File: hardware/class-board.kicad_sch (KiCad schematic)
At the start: 0 parts

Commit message: hardware: panel stacked on the back (180 x 100, three 2x20 headers, 17 SMA, TTL strip, TX terminal, Qwiic); TTL/fast/TX-coil/Qwiic connectors leave the main board; mains-safe relay channels (JQC-3FF 10 A, MAINS net class + DRC rules); library, sheets, gapped copies, docs regenerated; ERC 0 errors
Decisions #45-#50 in the course repo. The main-board PCB is unchanged: Update PCB from Schematic, header placement, relay re-spacing and connector rotation are the instructor's GUI steps on the master.

Co-Authored-By: Claude Fable 5.1 <noreply@anthropic.com>
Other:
- note added: "400 kHz: OLED 0x3C, TCA9535 0x20, Si5351A 0x60, Qwiic J4 + panel Qwiic"
- note added: "74AHCT541 -> 1 k -> panel link -> panel TTL strip"
- note added: "74HCT125 -> 49.9 R -> panel link -> 2 fast SMAs on the panel"
- note added: "74LVC1T45; DIR 1 = output to the panel SMA"
- note added: "<= 1.5 A (est. 1.15-1.35 A)"
- note added: "L1/L4 analog copper, panel copper (through J6)"
- note added: "LINK: 3 x 2x20 to the front panel (bottom side)"
- note added: "Stack-up: L1 signal/power, L2 GND, L3 GND, L4 signal/power. Board 180 x 100 mm, 4 x M3. Bottom side: three 2x20 straight male headers (J6 at x 12, J7 at x 90, J8 at x 168 mm) carry the front panel (180 x 100, 17 SMA) flat on the back of the board. Rear edge: USB-C, 5 V jack, relay contacts, isolated inputs, external power, H-bridge and polarizer coil terminals. Sections: A = B1 + NMR RX, B = B3 +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"
- note added: "dev board, relays (4 x 71 mA), 5 V logic, LDO, DC-DC"
- note removed: "400 kHz: OLED 0x3C, TCA9535 0x20, Si5351A 0x60, 2 Qwiic"
- note removed: "74AHCT541 -> 1 k -> terminals (I2C expander)"
- note removed: "74HCT125 -> 49.9 R -> terminals"
- note removed: "74LVC1T45; DIR 1 = output to the SMA"
- note removed: "<= 1.5 A (est. 1.0-1.2 A)"
- note removed: "L1/L4 analog copper, panel copper"
- note removed: "LINK: 2x20 to the front panel"
- note removed: "Stack-up: L1 signal/power, L2 GND, L3 GND, L4 signal/power. Board 160 x 100 mm, 4 x M3. Front edge: 2x20 link to the SMA/OLED/LED panel (160 x 65, 3 x 5 SMA). Rear edge: USB-C, 5 V jack, terminals, external power. Sections: A = B1 + NMR RX, B = B3 + B5 + NMR TX, C = B2 + B4 + coil switches."
- note removed: "dev board, relays, 5 V logic, LDO, DC-DC"
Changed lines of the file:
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@@
   (text "TIGP CLASS BOARD 2026 — laboratory instrument carrier (ESP32-S3 dev board) with NMR console, rev B (v0.7, 2026-09-13)" (exclude_from_sim no) (at 12.7 16 0) (effects (font (size 3.5 3.5) (bold yes)) (justify left bottom)))
   (text "Design brief v0.6 + notes/2026-09-13-nmr-respec-proposal.md (v0.7) + hardware/docs/design-decisions.md. Interface nets between sheets are global labels; rails are power symbols; AGND meets GND only at NT1." (exclude_from_sim no) (at 12.7 21 0) (effects (font (size 1.5 1.5)) (justify left bottom)))
-  (text "Stack-up: L1 signal/power, L2 GND, L3 GND, L4 signal/power. Board 160 x 100 mm, 4 x M3. Front edge: 2x20 link to the SMA/OLED/LED panel (160 x 65, 3 x 5 SMA). Rear edge: USB-C, 5 V jack, terminals, external power. Sections: A = B1 + NMR RX, B = B3 + B5 + NMR TX, C = B2 + B4 + coil switches." (exclude_from_sim no) (at 12.7 25 0) (effects (font (size 1.5 1.5)) (justify left bottom)))
+  (text "Stack-up: L1 signal/power, L2 GND, L3 GND, L4 signal/power. Board 180 x 100 mm, 4 x M3. Bottom side: three 2x20 straight male headers (J6 at x 12, J7 at x 90, J8 at x 168 mm) carry the front panel (180 x 100, 17 SMA) flat on the back of the board. Rear edge: USB-C, 5 V jack, relay contacts, isolated inputs, external power, H-bridge and polarizer coil terminals. Sections: A = B1 + NMR RX, B = B3 + B5 + NMR TX, C = B2 + B4 + coil switches." (exclude_from_sim no) (at 12.7 25 0) (effects (font (size 1.5 1.5)) (justify left bottom)))
   (text "BASE: dev-board socket, buses, expansion, star point" (exclude_from_sim no) (at 14.2 62 0) (effects (font (size 1.3 1.3)) (justify left bottom)))
   (text "B2 (C): power entry, +-12 V, LDOs" (exclude_from_sim no) (at 114.2 62 0) (effects (font (size 1.3 1.3)) (justify left bottom)))
@@
   (text "B4 (C): 4 relays, 2 isolated inputs" (exclude_from_sim no) (at 14.2 107 0) (effects (font (size 1.3 1.3)) (justify left bottom)))
   (text "B5 (B): TCA9535 -> 8 TTL DIO + relays, 2 fast outs, TRIG" (exclude_from_sim no) (at 114.2 107 0) (effects (font (size 1.3 1.3)) (justify left bottom)))
-  (text "LINK: 2x20 to the front panel" (exclude_from_sim no) (at 214.2 107 0) (effects (font (size 1.3 1.3)) (justify left bottom)))
+  (text "LINK: 3 x 2x20 to the front panel (bottom side)" (exclude_from_sim no) (at 214.2 107 0) (effects (font (size 1.3 1.3)) (justify left bottom)))
   (text "C: external power input, DRV8871 field-cycling H-bridge, polarizer MOSFET switch" (exclude_from_sim no) (at 314.2 107 0) (effects (font (size 1.3 1.3)) (justify left bottom)))
   (text "NMR RX (A): tank, LNA, blanking, I/Q mixer, IF -> ADC ch 7/8" (exclude_from_sim no) (at 14.2 152 0) (effects (font (size 1.3 1.3)) (justify left bottom)))
@@
   (text "1/2" (exclude_from_sim no) (at 13.5 193.4992 0) (effects (font (size 1.3 1.3)) (justify left bottom)))
   (text "I2C_SDA/SCL" (exclude_from_sim no) (at 47.5 193.4992 0) (effects (font (size 1.3 1.3)) (justify left bottom)))
-  (text "400 kHz: OLED 0x3C, TCA9535 0x20, Si5351A 0x60, 2 Qwiic" (exclude_from_sim no) (at 87.5 193.4992 0) (effects (font (size 1.3 1.3)) (justify left bottom)))
+  (text "400 kHz: OLED 0x3C, TCA9535 0x20, Si5351A 0x60, Qwiic J4 + panel Qwiic" (exclude_from_sim no) (at 87.5 193.4992 0) (effects (font (size 1.3 1.3)) (justify left bottom)))
   (text "base" (exclude_from_sim no) (at 179.5 193.4992 0) (effects (font (size 1.3 1.3)) (justify left bottom)))
   (text "16/17" (exclude_from_sim no) (at 13.5 196.3592 0) (effects (font (size 1.3 1.3)) (justify left bottom)))
@@
   (text "18/21" (exclude_from_sim no) (at 13.5 199.2192 0) (effects (font (size 1.3 1.3)) (justify left bottom)))
   (text "FAST_OUT1/2" (exclude_from_sim no) (at 47.5 199.2192 0) (effects (font (size 1.3 1.3)) (justify left bottom)))
-  (text "74HCT125 -> 49.9 R -> terminals" (exclude_from_sim no) (at 87.5 199.2192 0) (effects (font (size 1.3 1.3)) (justify left bottom)))
+  (text "74HCT125 -> 49.9 R -> panel link -> 2 fast SMAs on the panel" (exclude_from_sim no) (at 87.5 199.2192 0) (effects (font (size 1.3 1.3)) (justify left bottom)))
   (text "B" (exclude_from_sim no) (at 179.5 199.2192 0) (effects (font (size 1.3 1.3)) (justify left bottom)))
   (text "38/39" (exclude_from_sim no) (at 13.5 202.0792 0) (effects (font (size 1.3 1.3)) (justify left bottom)))
   (text "TRIG_IO / TRIG_DIR" (exclude_from_sim no) (at 47.5 202.0792 0) (effects (font (size 1.3 1.3)) (justify left bottom)))
-  (text "74LVC1T45; DIR 1 = output to the SMA" (exclude_from_sim no) (at 87.5 202.0792 0) (effects (font (size 1.3 1.3)) (justify left bottom)))
+  (text "74LVC1T45; DIR 1 = output to the panel SMA" (exclude_from_sim no) (at 87.5 202.0792 0) (effects (font (size 1.3 1.3)) (justify left bottom)))
   (text "B" (exclude_from_sim no) (at 179.5 202.0792 0) (effects (font (size 1.3 1.3)) (justify left bottom)))
   (text "41/42" (exclude_from_sim no) (at 13.5 204.9392 0) (effects (font (size 1.3 1.3)) (justify left bottom)))
@@
   (text "TCA9535 P00-P07" (exclude_from_sim no) (at 13.5 219.2392 0) (effects (font (size 1.3 1.3)) (justify left bottom)))
   (text "DIO1..8" (exclude_from_sim no) (at 47.5 219.2392 0) (effects (font (size 1.3 1.3)) (justify left bottom)))
-  (text "74AHCT541 -> 1 k -> terminals (I2C expander)" (exclude_from_sim no) (at 87.5 219.2392 0) (effects (font (size 1.3 1.3)) (justify left bottom)))
+  (text "74AHCT541 -> 1 k -> panel link -> panel TTL strip" (exclude_from_sim no) (at 87.5 219.2392 0) (effects (font (size 1.3 1.3)) (justify left bottom)))
   (text "B" (exclude_from_sim no) (at 179.5 219.2392 0) (effects (font (size 1.3 1.3)) (justify left bottom)))
   (text "TCA9535 P10-P13" (exclude_from_sim no) (at 13.5 222.0992 0) (effects (font (size 1.3 1.3)) (justify left bottom)))
@@
   (text "+5V_RAW" (exclude_from_sim no) (at 200.8 184.9192 0) (effects (font (size 1.3 1.3)) (justify left bottom)))
   (text "USB-C or jack via polyfuse + TVS + LM66100" (exclude_from_sim no) (at 226.8 184.9192 0) (effects (font (size 1.3 1.3)) (justify left bottom)))
-  (text "<= 1.5 A (est. 1.0-1.2 A)" (exclude_from_sim no) (at 288.8 184.9192 0) (effects (font (size 1.3 1.3)) (justify left bottom)))
-  (text "dev board, relays, 5 V logic, LDO, DC-DC" (exclude_from_sim no) (at 340.8 184.9192 0) (effects (font (size 1.3 1.3)) (justify left bottom)))
+  (text "<= 1.5 A (est. 1.15-1.35 A)" (exclude_from_sim no) (at 288.8 184.9192 0) (effects (font (size 1.3 1.3)) (justify left bottom)))
+  (text "dev board, relays (4 x 71 mA), 5 V logic, LDO, DC-DC" (exclude_from_sim no) (at 340.8 184.9192 0) (effects (font (size 1.3 1.3)) (justify left bottom)))
   (text "+3V3" (exclude_from_sim no) (at 200.8 187.7792 0) (effects (font (size 1.3 1.3)) (justify left bottom)))
   (text "AMS1117-3.3" (exclude_from_sim no) (at 226.8 187.7792 0) (effects (font (size 1.3 1.3)) (justify left bottom)))
@@
   (text "star point NT1 (net tie) to GND" (exclude_from_sim no) (at 226.8 196.3592 0) (effects (font (size 1.3 1.3)) (justify left bottom)))
   (text "-" (exclude_from_sim no) (at 288.8 196.3592 0) (effects (font (size 1.3 1.3)) (justify left bottom)))
-  (text "L1/L4 analog copper, panel copper" (exclude_from_sim no) (at 340.8 196.3592 0) (effects (font (size 1.3 1.3)) (justify left bottom)))
+  (text "L1/L4 analog copper, panel copper (through J6)" (exclude_from_sim no) (at 340.8 196.3592 0) (effects (font (size 1.3 1.3)) (justify left bottom)))
   (sheet (at 12.7 35.56) (size 88.9 30.48) (fields_autoplaced yes) (stroke (width 0.1524) (type solid)) (fill (color 0 0 0 0.0000))
     (property "Sheetname" "base_mcu" (at 12.7 34.86 0) (effects (font (size 1.5 1.5) (bold yes)) (justify left bottom)))

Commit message: v0.7d: relays and mains removed, MODULE OUT 1-7 (5 V TTL) on a shrouded 2x6 header on the front panel, isolated inputs moved to the panel, section C = the front-panel board (4-layer, 18 mm SMA grid, OLED clear of headers, unrouted student copy), main board re-placed; workbook, tutor guide, firmware docs, hardware docs updated (Decision #58)
Co-Authored-By: Claude Fable 5.1 <noreply@anthropic.com>
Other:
- removed sheet b4_switching
- note added: "/CLR of the 74HC74 Johnson counter (NMR RX); TP501"
- note added: "3.3 V -> panel link J8 -> 5 V TTL buffers on the panel (OUT 8 reserved, J8 pin 33 n/c)"
- note added: "<= 1.5 A (est. 0.87-1.07 A)"
- note added: "B5 (B): TCA9535 -> 8 TTL DIO + 8 module outputs, 2 fast outs, TRIG"
- note added: "EXP_P14"
- note added: "MODULE OUT 1..7"
- note added: "Reference ranges: base 1-99, B1 100-199, B2 200-299, B3 300-399, B5 500-599, NMR RX 700-799, NMR TX 800-899, coil switches / external power 900-999. B4 (400-499, relays and isolated inputs) was deleted in v0.7d; the owner-zone DRC uses the Block field."
- note added: "Stack-up: L1 signal/power, L2 GND, L3 GND, L4 signal/power. Board 180 x 100 mm, 4 x M3. Bottom side: three 2x20 straight male headers (J6 at x 12, J7 at x 90, J8 at x 168 mm) carry the front panel (180 x 100, 17 SMA) flat on the back of the board. Rear edge: USB-C, 5 V jack, external power, H-bridge and polarizer coil terminals. Sections: A = B1 + NMR RX, B = B3 + B5 + NMR TX, C = the front-panel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"
- note added: "TCA9535 P10-P13, P15-P17"
- note added: "TCA9535 P14"
- note added: "dev board, 5 V logic, LDO, DC-DC, the panel through J8"
- note added: "panel"
- note added: "the two isolated inputs, now on the front panel; active LOW"
- note removed: "6N137 outputs, 1 k pull-up, active LOW"
- note removed: "<= 1.5 A (est. 1.15-1.35 A)"
- note removed: "AO3400A relay gates (10 k pull-down)"
- note removed: "B4 (C): 4 relays, 2 isolated inputs"
- note removed: "B5 (B): TCA9535 -> 8 TTL DIO + relays, 2 fast outs, TRIG"
- note removed: "RLY_IN1..4"
- note removed: "Reference ranges: base 1-99, B1 100-199, B2 200-299, B3 300-399, B4 400-499, B5 500-599, NMR RX 700-799, NMR TX 800-899, coil switches / external power 900-999 (owner-zone DRC uses the Block field: A / B / C)."
- note removed: "Stack-up: L1 signal/power, L2 GND, L3 GND, L4 signal/power. Board 180 x 100 mm, 4 x M3. Bottom side: three 2x20 straight male headers (J6 at x 12, J7 at x 90, J8 at x 168 mm) carry the front panel (180 x 100, 17 SMA) flat on the back of the board. Rear edge: USB-C, 5 V jack, relay contacts, isolated inputs, external power, H-bridge and polarizer coil terminals. Sections: A = B1 + NMR RX, B = B3 +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"
- note removed: "TCA9535 P10-P13"
- note removed: "dev board, relays (4 x 71 mA), 5 V logic, LDO, DC-DC"

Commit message: Boards as hand-reworked by the instructor 2026-09-18 (Decision #66): three 2x20 links re-placed, jumpers -> headers, TCXO removed, 16 SMA; layout and routing in progress; review in the course repo notes
Co-Authored-By: Claude Fable 5.1 <noreply@anthropic.com>
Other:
- sheet b1_inputs ports: added AO1, AO2, AUX, COND_OUT1, COND_OUT2, CS_ADC, RX, TX; removed none
- sheet b2_power ports: added USB_D_N, USB_D_P; removed none
- sheet b3_outputs ports: added AO1, AO2, CS_DAC; removed none
- sheet b5_dio_trig ports: added EXP_P14, FAST_OUT1, FAST_OUT2, LED_ACT, LED_WIFI, OPTO_IN1, OPTO_IN2, TRIG_DIR, TRIG_IO; removed none
- sheet base_mcu ports: added CS_ADC, CS_DAC, DDS_FSYNC, DDS_PSEL, FAST_OUT1, FAST_OUT2, FET_GATE, HB_IN1, HB_IN2, LED_ACT, LED_WIFI, OPTO_IN1, OPTO_IN2, RX_BLANK, TRIG_DIR, TRIG_IO, TX_EN, USB_D_N, USB_D_P; removed none
- sheet c_switch ports: added FET_GATE, HB_IN1, HB_IN2; removed none
- sheet nmr_rx ports: added AUX, CLK0_MCLK, COND_OUT1, COND_OUT2, EXP_P14, RX, RX_BLANK; removed none
- sheet nmr_tx ports: added CLK0_MCLK, DDS_FSYNC, DDS_PSEL, TX, TX_EN; removed none

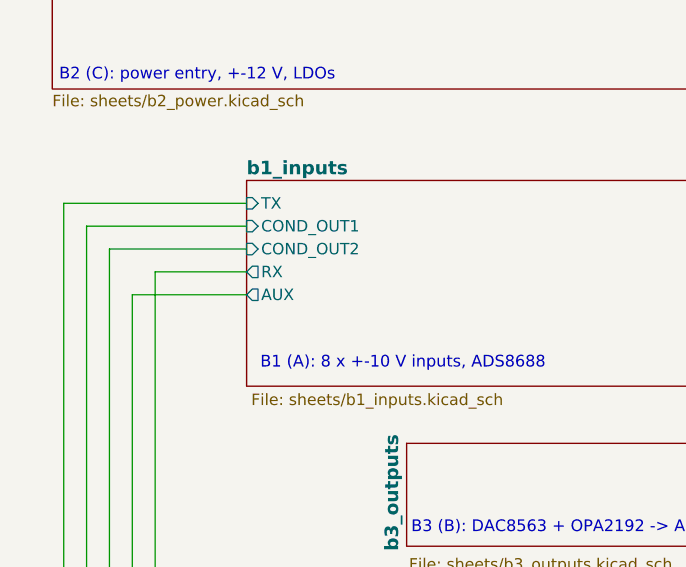
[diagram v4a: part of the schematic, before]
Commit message: Schematic review fixes, part 1 (branch, not merged): root sheet RX/AUX un-crossed + b1_inputs J6 pin 20/22 labels swapped (copper unchanged); firmware: ADC channel table kAinOfAi, FAST_OUT pins, module outputs 1-7 (relay -> module per PROTOCOL.md), AD9834 PIN/SW = 0, opto INPUT_PULLUP, stale comments; both PlatformIO envs build
Co-Authored-By: Claude Fable 5.1 <noreply@anthropic.com>
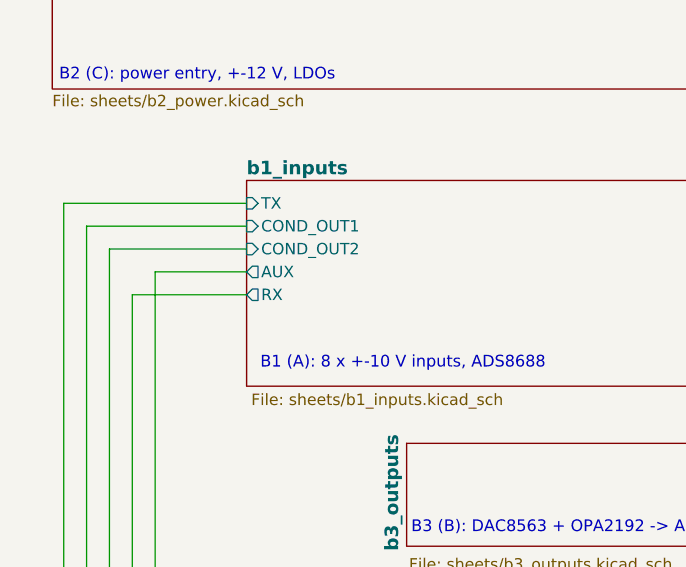
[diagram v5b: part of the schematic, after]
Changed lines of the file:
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@@
 			)
 		)
-		(pin "AUX" output
+		(pin "RX" output
 			(at 43.18 86.36 180)
 			(effects
@@
 			)
 		)
-		(pin "RX" output
+		(pin "AUX" output
 			(at 43.18 83.82 180)
 			(effects

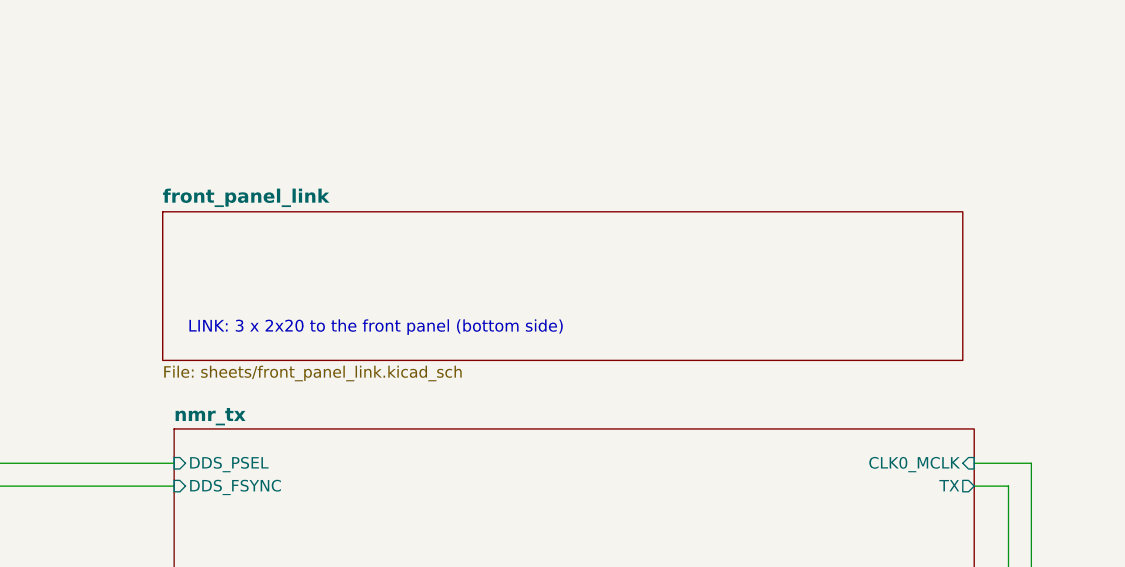
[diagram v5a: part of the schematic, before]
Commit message: Schematic review fixes, part 2 (Konnect): panel RX/AUX labels + SMA labels swapped to match the main board (copper unchanged); TX_VMID -> R820 47k -> TX_IN (C810 couples into TX_IN); Q901 D/S corrected + D932 to +VEXT; R950 10k Q904 gate-source; R712 permanent (J3 pin 1 tied to pin 2); U302/C308 on +5VA; panel 6N137 VCC/VE + C401/C402 on +5V_RAW; R521-R528 DIO pull-downs; front_panel_link sheet removed from the root; change notes on six sheets; panel silk: pairing labels corrected, stale J3 texts deleted, TX/RX/AUX labels fixed, OUT1..7. ERC unchanged (2 cosmetic), panel DRC 0/0; netlist diff = intended changes only
Co-Authored-By: Claude Fable 5.1 <noreply@anthropic.com>
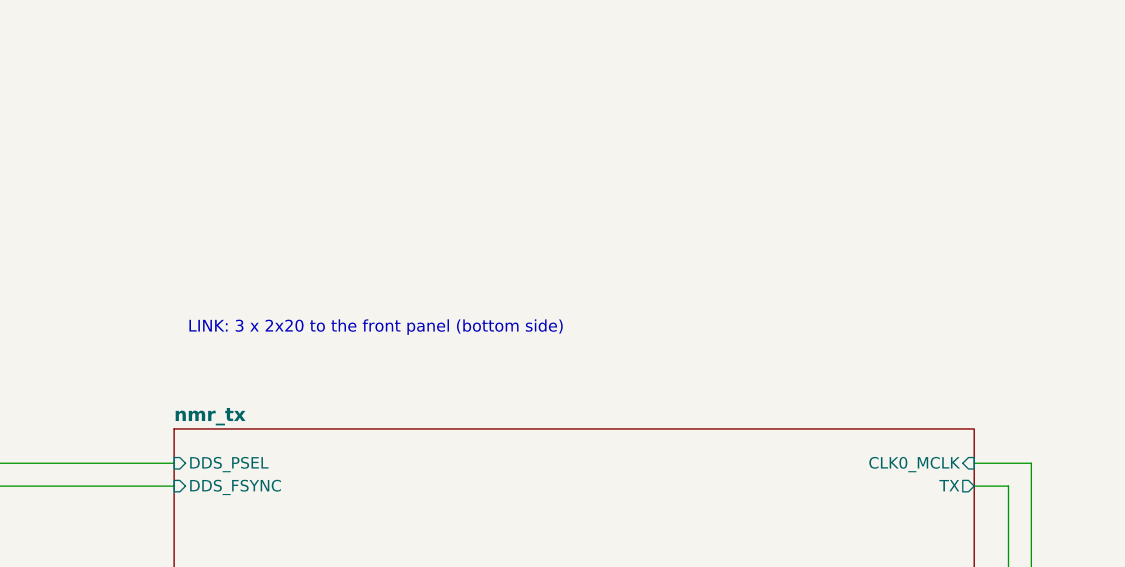
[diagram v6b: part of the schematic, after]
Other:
- removed sheet front_panel_link
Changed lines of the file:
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@@
-	)
-	(sheet
-		(at 270.51 49.53)
-		(size 88.9 16.51)
-		(exclude_from_sim no)
-		(in_bom yes)
-		(on_board yes)
-		(dnp no)
-		(fields_autoplaced yes)
-		(stroke
-			(width 0.1524)
-			(type solid)
-		)
-		(fill
-			(color 0 0 0 0)
-		)
-		(property "Sheetname" "front_panel_link"
-			(at 270.51 48.7034 0)
-			(show_name no)
-			(do_not_autoplace no)
-			(effects
-				(font
-					(size 1.5 1.5)
-					(bold yes)
-				)
-				(justify left bottom)
-			)
-		)
-		(property "Sheetfile" "sheets/front_panel_link.kicad_sch"
-			(at 270.51 66.6246 0)
-			(show_name no)
-			(do_not_autoplace no)
-			(effects
-				(font
-					(size 1.27 1.27)
-				)
-				(justify left top)
-			)
-		)
-		(instances
-			(project "class-board"
-				(path "/21416d14-3056-576f-bbf8-3b43eaeb7e71"
-					(page "9")
-				)
-			)
-		)
 	)
 	(sheet
